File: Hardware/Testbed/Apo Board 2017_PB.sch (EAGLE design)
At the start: 23 parts, among them J1 AVR_SPI_PROG_3X2PTH, J2 AVR_SPI_PROG_3X2PTH, J3 POWER_JACK

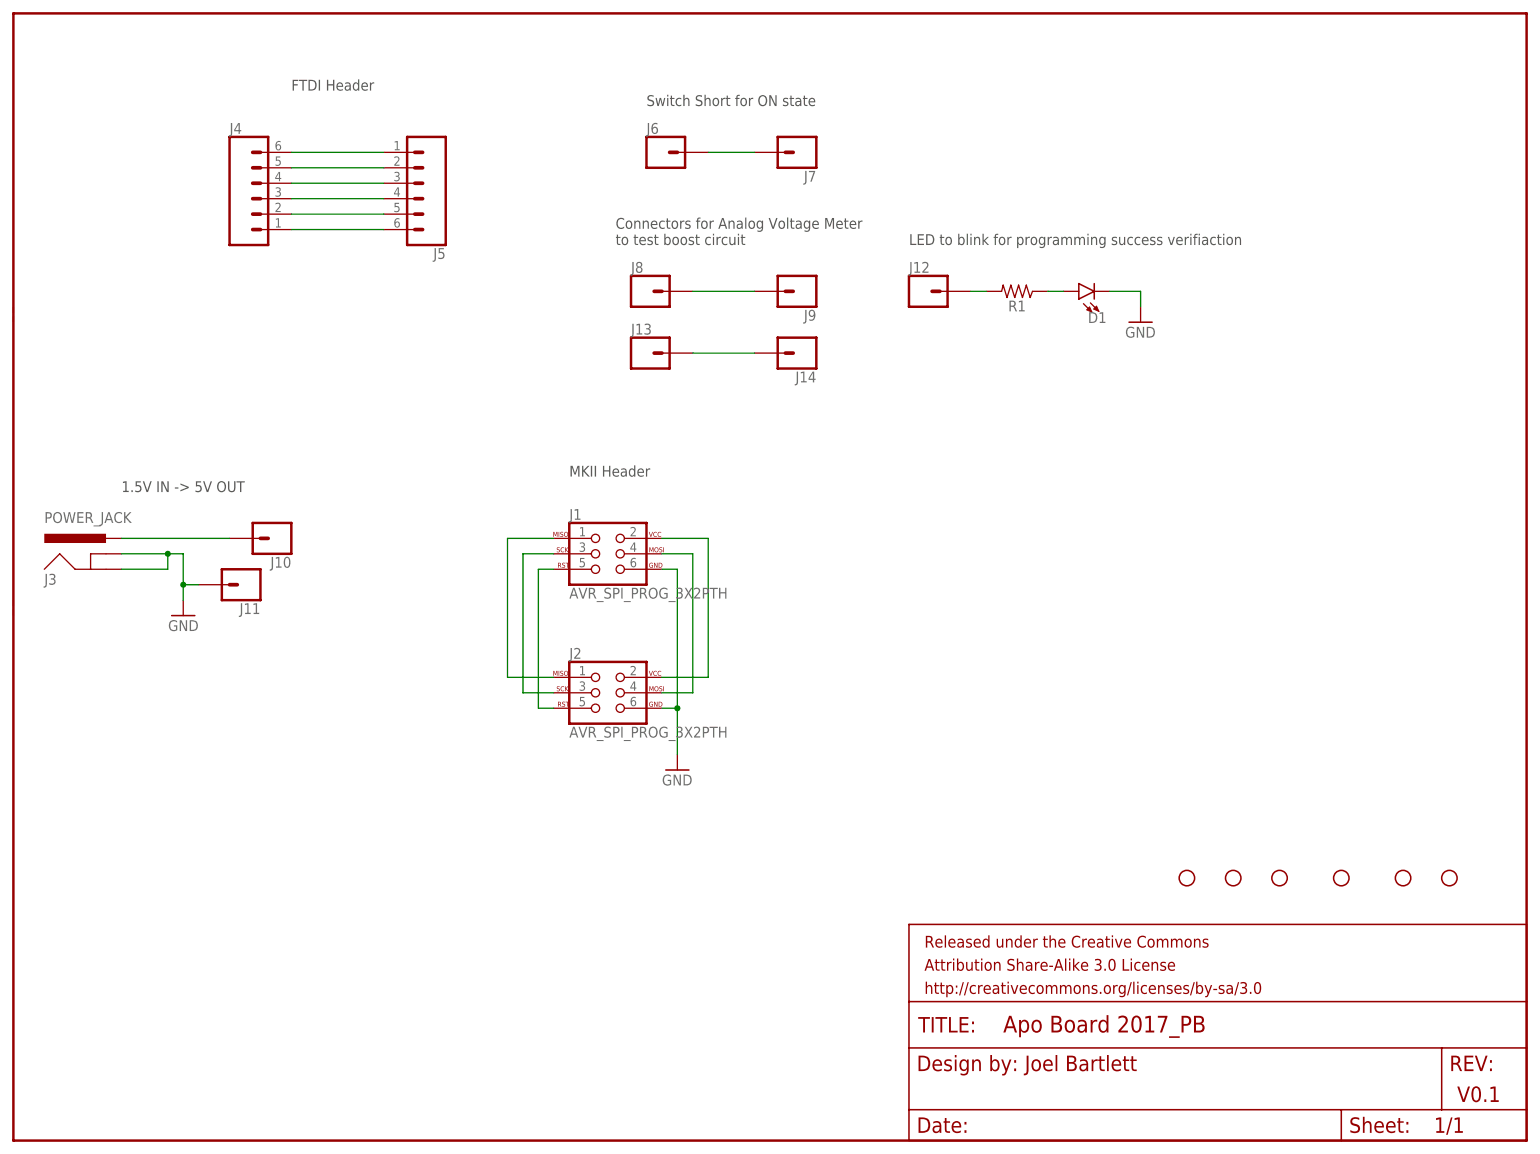
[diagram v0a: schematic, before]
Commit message: Pogo Bed finished.
Finished making pogoed programming and testing fixture. Moving to
Hardware Folder
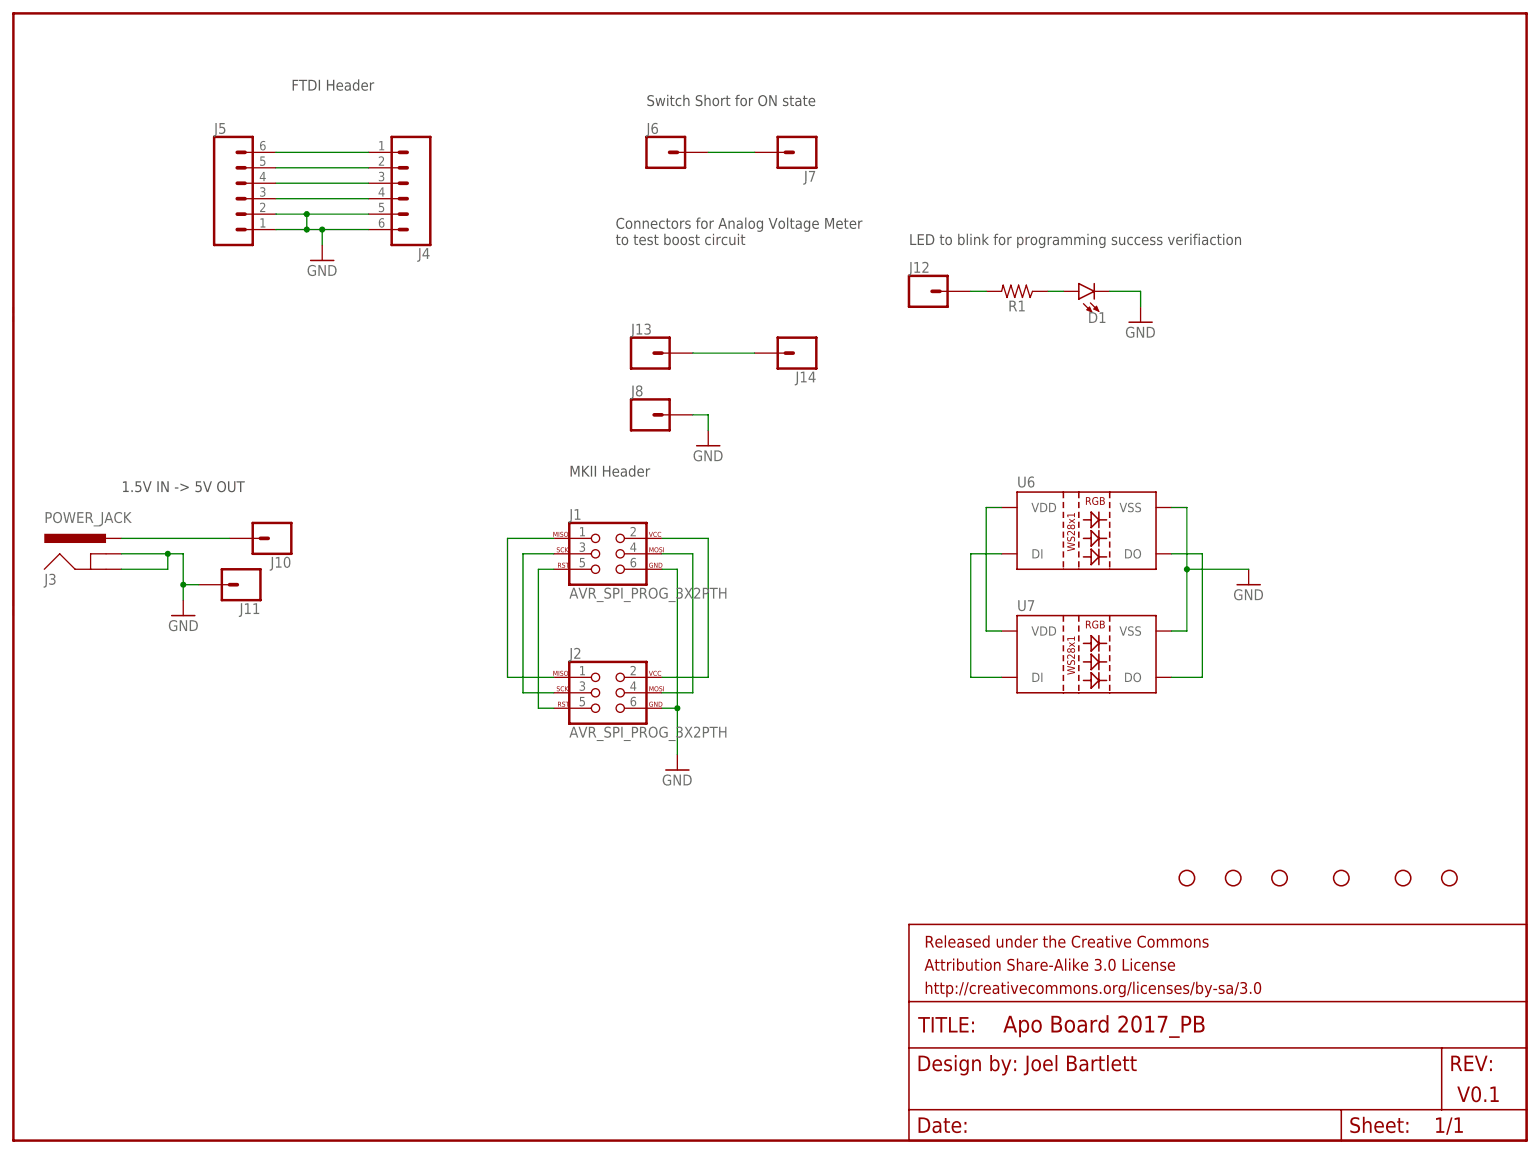
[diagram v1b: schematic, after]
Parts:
- removed J9: (no value), SparkFun-Connectors:CONN_01PTH_LONGPAD
- added U6, U7: LED-TRICOLOR-5050-ICWS2812-THRU-KIT, SparkFun-LED:LED-TRICOLOR-5050-ICWS2812-THRU-KIT
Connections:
- removed net N$8: J4.5, J5.2
- new net N$18: U6.VDD, U7.VDD
- net GND: now also J4.5, J4.6, J5.1, J5.2, J8.1, U6.VSS, U7.VSS
- net N$16: now also U6.DI, U7.DI; no longer J8.1, J9.1
- net N$7: now also U6.DO, U7.DO; no longer J4.6, J5.1
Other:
- moved on the sheet: J4, J5, J8
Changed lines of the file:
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@@
 <part name="J7" library="SparkFun-Connectors" deviceset="CONN_01" device="PTH_LONGPAD"/>
 <part name="J8" library="SparkFun-Connectors" deviceset="CONN_01" device="PTH_LONGPAD"/>
-<part name="J9" library="SparkFun-Connectors" deviceset="CONN_01" device="PTH_LONGPAD"/>
 <part name="J10" library="SparkFun-Connectors" deviceset="CONN_01" device="PTH_LONGPAD"/>
 <part name="J11" library="SparkFun-Connectors" deviceset="CONN_01" device="PTH_LONGPAD"/>
@@
 <part name="J13" library="SparkFun-Connectors" deviceset="CONN_01" device="PTH_LONGPAD"/>
 <part name="J14" library="SparkFun-Connectors" deviceset="CONN_01" device="PTH_LONGPAD"/>
+<part name="GND2" library="SparkFun-Aesthetics" deviceset="GND" device=""/>
+<part name="GND4" library="SparkFun-Aesthetics" deviceset="GND" device=""/>
+<part name="U6" library="SparkFun-LED" deviceset="LED-TRICOLOR-5050-IC" device="WS2812-THRU-KIT" value=""/>
+<part name="U7" library="SparkFun-LED" deviceset="LED-TRICOLOR-5050-IC" device="WS2812-THRU-KIT" value=""/>
+<part name="GND5" library="SparkFun-Aesthetics" deviceset="GND" device=""/>
 </parts>
 <sheets>
@@
 <instance part="H5" gate="G$1" x="228.6" y="43.18"/>
 <instance part="H6" gate="G$1" x="236.22" y="43.18"/>
-<instance part="J4" gate="G$1" x="40.64" y="154.94"/>
-<instance part="J5" gate="G$1" x="66.04" y="157.48" rot="R180"/>
+<instance part="J4" gate="G$1" x="63.5" y="157.48" rot="R180"/>
+<instance part="J5" gate="G$1" x="38.1" y="154.94"/>
 <instance part="J6" gate="G$1" x="106.68" y="162.56"/>
 <instance part="J7" gate="G$1" x="129.54" y="162.56" rot="R180"/>
-<instance part="J8" gate="G$1" x="104.14" y="139.7"/>
-<instance part="J9" gate="G$1" x="129.54" y="139.7" rot="R180"/>
+<instance part="J8" gate="G$1" x="104.14" y="119.38"/>
 <instance part="J10" gate="G$1" x="43.18" y="99.06" rot="R180"/>
 <instance part="J11" gate="G$1" x="38.1" y="91.44" rot="R180"/>
@@
 <instance part="J13" gate="G$1" x="104.14" y="129.54"/>
 <instance part="J14" gate="G$1" x="129.54" y="129.54" rot="R180"/>
+<instance part="GND2" gate="1" x="114.3" y="114.3"/>
+<instance part="GND4" gate="1" x="50.8" y="144.78"/>
+<instance part="U6" gate="U1" x="177.8" y="99.06"/>
+<instance part="U7" gate="U1" x="177.8" y="78.74"/>
+<instance part="GND5" gate="1" x="203.2" y="91.44"/>
 </instances>
 <busses>
@@
 <wire x1="185.42" y1="139.7" x2="185.42" y2="137.16" width="0.1524" layer="91"/>
 </segment>
+<segment>
+<pinref part="GND2" gate="1" pin="GND"/>
+<pinref part="J8" gate="G$1" pin="1"/>
+<wire x1="114.3" y1="116.84" x2="114.3" y2="119.38" width="0.1524" layer="91"/>
+<wire x1="114.3" y1="119.38" x2="111.76" y2="119.38" width="0.1524" layer="91"/>
+</segment>
+<segment>
+<pinref part="J4" gate="G$1" pin="6"/>
+<pinref part="J5" gate="G$1" pin="1"/>
+<wire x1="43.18" y1="149.86" x2="48.26" y2="149.86" width="0.1524" layer="91"/>
+<pinref part="GND4" gate="1" pin="GND"/>
+<wire x1="48.26" y1="149.86" x2="50.8" y2="149.86" width="0.1524" layer="91"/>
+<wire x1="50.8" y1="149.86" x2="58.42" y2="149.86" width="0.1524" layer="91"/>
+<wire x1="50.8" y1="147.32" x2="50.8" y2="149.86" width="0.1524" layer="91"/>
+<junction x="50.8" y="149.86"/>
+<pinref part="J4" gate="G$1" pin="5"/>
+<pinref part="J5" gate="G$1" pin="2"/>
+<wire x1="43.18" y1="152.4" x2="48.26" y2="152.4" width="0.1524" layer="91"/>
+<wire x1="48.26" y1="152.4" x2="58.42" y2="152.4" width="0.1524" layer="91"/>
+<wire x1="48.26" y1="149.86" x2="48.26" y2="152.4" width="0.1524" layer="91"/>
+<junction x="48.26" y="149.86"/>
+<junction x="48.26" y="152.4"/>
+</segment>
+<segment>
+<pinref part="U7" gate="U1" pin="VSS"/>
+<wire x1="190.5" y1="83.82" x2="193.04" y2="83.82" width="0.1524" layer="91"/>
+<wire x1="193.04" y1="83.82" x2="193.04" y2="93.98" width="0.1524" layer="91"/>
+<pinref part="U6" gate="U1" pin="VSS"/>
+<wire x1="193.04" y1="93.98" x2="193.04" y2="104.14" width="0.1524" layer="91"/>
+<wire x1="193.04" y1="104.14" x2="190.5" y2="104.14" width="0.1524" layer="91"/>
+<pinref part="GND5" gate="1" pin="GND"/>
+<wire x1="203.2" y1="93.98" x2="193.04" y2="93.98" width="0.1524" layer="91"/>
+<junction x="193.04" y="93.98"/>
+</segment>
 </net>
 <net name="N$2" class="0">
@@
 </segment>
 </net>
-<net name="N$7" class="0">
-<segment>
-<pinref part="J4" gate="G$1" pin="6"/>
-<pinref part="J5" gate="G$1" pin="1"/>
-<wire x1="60.96" y1="162.56" x2="45.72" y2="162.56" width="0.1524" layer="91"/>
-</segment>
-</net>
-<net name="N$8" class="0">
-<segment>
-<pinref part="J4" gate="G$1" pin="5"/>
-<pinref part="J5" gate="G$1" pin="2"/>
-<wire x1="60.96" y1="160.02" x2="45.72" y2="160.02" width="0.1524" layer="91"/>
-</segment>
-</net>
 <net name="N$9" class="0">
 <segment>
 <pinref part="J4" gate="G$1" pin="4"/>
 <pinref part="J5" gate="G$1" pin="3"/>
-<wire x1="60.96" y1="157.48" x2="45.72" y2="157.48" width="0.1524" layer="91"/>
+<wire x1="43.18" y1="154.94" x2="58.42" y2="154.94" width="0.1524" layer="91"/>
 </segment>
 </net>
@@
 <pinref part="J4" gate="G$1" pin="3"/>
 <pinref part="J5" gate="G$1" pin="4"/>
-<wire x1="60.96" y1="154.94" x2="45.72" y2="154.94" width="0.1524" layer="91"/>
+<wire x1="43.18" y1="157.48" x2="58.42" y2="157.48" width="0.1524" layer="91"/>
 </segment>
 </net>
@@
 <pinref part="J4" gate="G$1" pin="2"/>
 <pinref part="J5" gate="G$1" pin="5"/>
-<wire x1="60.96" y1="152.4" x2="45.72" y2="152.4" width="0.1524" layer="91"/>
+<wire x1="43.18" y1="160.02" x2="58.42" y2="160.02" width="0.1524" layer="91"/>
 </segment>
 </net>
@@
 <pinref part="J4" gate="G$1" pin="1"/>
 <pinref part="J5" gate="G$1" pin="6"/>
-<wire x1="60.96" y1="149.86" x2="45.72" y2="149.86" width="0.1524" layer="91"/>
+<wire x1="43.18" y1="162.56" x2="58.42" y2="162.56" width="0.1524" layer="91"/>
 </segment>
 </net>
@@
 </segment>
 </net>
-<net name="N$16" class="0">
-<segment>
-<pinref part="J9" gate="G$1" pin="1"/>
-<pinref part="J8" gate="G$1" pin="1"/>
-<wire x1="111.76" y1="139.7" x2="121.92" y2="139.7" width="0.1524" layer="91"/>
-</segment>
-</net>
 <net name="N$17" class="0">
 <segment>
@@
 </segment>
 </net>
+<net name="N$7" class="0">
+<segment>
+<pinref part="U6" gate="U1" pin="DO"/>
+<wire x1="190.5" y1="96.52" x2="195.58" y2="96.52" width="0.1524" layer="91"/>
+<wire x1="195.58" y1="96.52" x2="195.58" y2="76.2" width="0.1524" layer="91"/>
+<pinref part="U7" gate="U1" pin="DO"/>
+<wire x1="195.58" y1="76.2" x2="190.5" y2="76.2" width="0.1524" layer="91"/>
+</segment>
+</net>
+<net name="N$16" class="0">
+<segment>
+<pinref part="U6" gate="U1" pin="DI"/>
+<wire x1="162.56" y1="96.52" x2="157.48" y2="96.52" width="0.1524" layer="91"/>
+<wire x1="157.48" y1="96.52" x2="157.48" y2="76.2" width="0.1524" layer="91"/>
+<pinref part="U7" gate="U1" pin="DI"/>
+<wire x1="157.48" y1="76.2" x2="162.56" y2="76.2" width="0.1524" layer="91"/>
+</segment>
+</net>
+<net name="N$18" class="0">
+<segment>
+<pinref part="U6" gate="U1" pin="VDD"/>
+<wire x1="162.56" y1="104.14" x2="160.02" y2="104.14" width="0.1524" layer="91"/>
+<wire x1="160.02" y1="104.14" x2="160.02" y2="83.82" width="0.1524" layer="91"/>
+<pinref part="U7" gate="U1" pin="VDD"/>
+<wire x1="160.02" y1="83.82" x2="162.56" y2="83.82" width="0.1524" layer="91"/>
+</segment>
+</net>
